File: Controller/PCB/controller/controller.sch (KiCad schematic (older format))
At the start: 66 parts

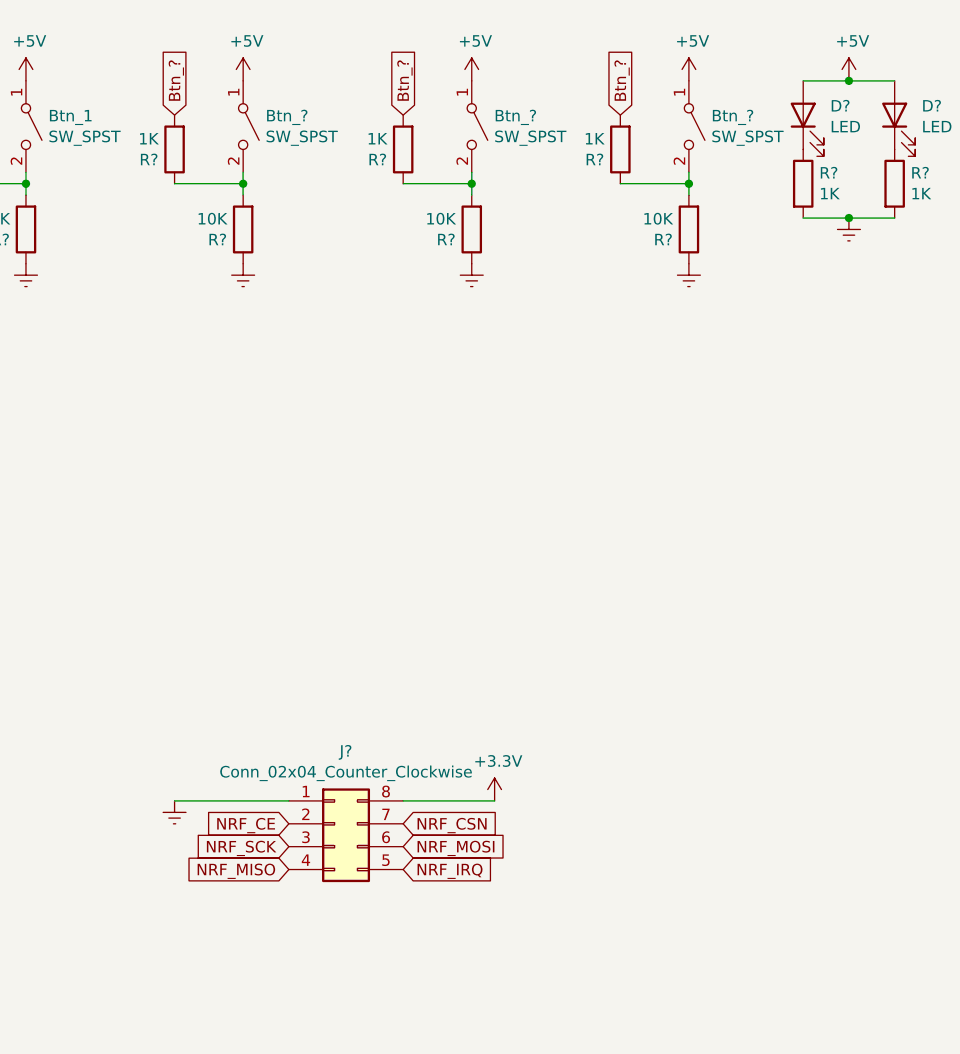
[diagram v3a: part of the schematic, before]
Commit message: Update 2 of the buttons into switches
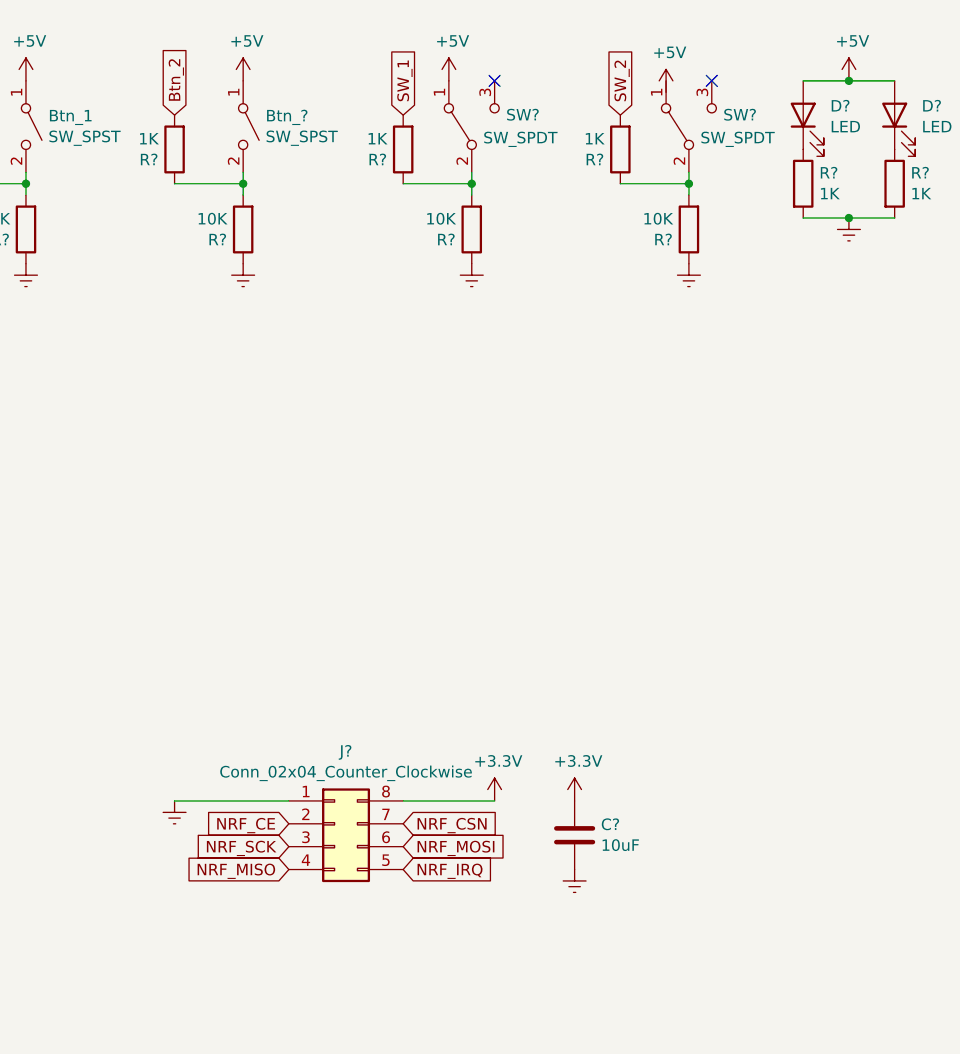
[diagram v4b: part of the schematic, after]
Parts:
- removed Btn_? (x2): SW_SPST, symbol Switch:SW_SPST
- added C?: 10uF, symbol Device:C
- added SW? (x2): SW_SPDT, symbol Switch:SW_SPDT
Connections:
- net +3V3: now also C?.1
- net +5V: now also SW?.1 (A)
- net Earth: now also C?.2
- net at R?.1, R?.2: now also SW?.2 (B) (x2)
- removed net Btn_?: R?.2, R?.2, R?.2
- new net Btn_2: R?.2
- new net SW_1: R?.2
- new net SW_2: R?.2
- no-connect marks 1 -> 3
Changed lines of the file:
@@
 $EndComp
 Text GLabel 6000 900  1    50   Input ~ 0
-Btn_?
+Btn_2
 $Comp
 L power:Earth #PWR?
@@
 Connection ~ 6300 1200
 $Comp
-L Switch:SW_SPST Btn_?
-U 1 1 6210AEE9
-P 7300 950
-F 0 "Btn_?" V 7254 1048 50  0000 L CNN
-F 1 "SW_SPST" V 7345 1048 50  0000 L CNN
-F 2 "" H 7300 950 50  0001 C CNN
-F 3 "~" H 7300 950 50  0001 C CNN
-	1    7300 950
-	0    1    1    0
-$EndComp
-$Comp
 L Device:R R?
 U 1 1 6210AEEF
@@
 $EndComp
 Text GLabel 7000 900  1    50   Input ~ 0
-Btn_?
+SW_1
 $Comp
 L power:Earth #PWR?
@@
 Connection ~ 7300 1200
 $Comp
-L Switch:SW_SPST Btn_?
-U 1 1 6210CFFF
-P 8250 950
-F 0 "Btn_?" V 8204 1048 50  0000 L CNN
-F 1 "SW_SPST" V 8295 1048 50  0000 L CNN
-F 2 "" H 8250 950 50  0001 C CNN
-F 3 "~" H 8250 950 50  0001 C CNN
-	1    8250 950
-	0    1    1    0
-$EndComp
-$Comp
 L Device:R R?
 U 1 1 6210D005
@@
 $EndComp
 Text GLabel 7950 900  1    50   Input ~ 0
-Btn_?
+SW_2
 $Comp
 L power:Earth #PWR?
@@
 L power:+5V #PWR?
 U 1 1 6208E5D4
-P 8250 750
-F 0 "#PWR?" H 8250 600 50  0001 C CNN
-F 1 "+5V" H 8265 923 50  0000 C CNN
-F 2 "" H 8250 750 50  0001 C CNN
-F 3 "" H 8250 750 50  0001 C CNN
-	1    8250 750
+P 8150 800
+F 0 "#PWR?" H 8150 650 50  0001 C CNN
+F 1 "+5V" H 8165 973 50  0000 C CNN
+F 2 "" H 8150 800 50  0001 C CNN
+F 3 "" H 8150 800 50  0001 C CNN
+	1    8150 800
 	1    0    0    -1
 $EndComp
@@
 L power:+5V #PWR?
 U 1 1 62091695
-P 7300 750
-F 0 "#PWR?" H 7300 600 50  0001 C CNN
-F 1 "+5V" H 7315 923 50  0000 C CNN
-F 2 "" H 7300 750 50  0001 C CNN
-F 3 "" H 7300 750 50  0001 C CNN
-	1    7300 750
+P 7200 750
+F 0 "#PWR?" H 7200 600 50  0001 C CNN
+F 1 "+5V" H 7215 923 50  0000 C CNN
+F 2 "" H 7200 750 50  0001 C CNN
+F 3 "" H 7200 750 50  0001 C CNN
+	1    7200 750
 	1    0    0    -1
 $EndComp
@@
 Text GLabel 7000 4000 2    50   Input ~ 0
 NRF_CSN
+$Comp
+L power:+3.3V #PWR?
+U 1 1 620F525F
+P 7750 3900
+F 0 "#PWR?" H 7750 3750 50  0001 C CNN
+F 1 "+3.3V" H 7765 4073 50  0000 C CNN
+F 2 "" H 7750 3900 50  0001 C CNN
+F 3 "" H 7750 3900 50  0001 C CNN
+	1    7750 3900
+	1    0    0    -1
+$EndComp
+$Comp
+L Device:C C?
+U 1 1 620F58B9
+P 7750 4050
+F 0 "C?" H 7865 4096 50  0000 L CNN
+F 1 "10uF" H 7865 4005 50  0000 L CNN
+F 2 "" H 7788 3900 50  0001 C CNN
+F 3 "~" H 7750 4050 50  0001 C CNN
+	1    7750 4050
+	1    0    0    -1
+$EndComp
+$Comp
+L power:Earth #PWR?
+U 1 1 620F67B9
+P 7750 4200
+F 0 "#PWR?" H 7750 3950 50  0001 C CNN
+F 1 "Earth" H 7750 4050 50  0001 C CNN
+F 2 "" H 7750 4200 50  0001 C CNN
+F 3 "~" H 7750 4200 50  0001 C CNN
+	1    7750 4200
+	1    0    0    -1
+$EndComp
+$Comp
+L Switch:SW_SPDT SW?
+U 1 1 620F8D01
+P 7300 950
+F 0 "SW?" V 7350 800 50  0000 R CNN
+F 1 "SW_SPDT" V 7250 900 50  0000 R CNN
+F 2 "" H 7300 950 50  0001 C CNN
+F 3 "~" H 7300 950 50  0001 C CNN
+	1    7300 950
+	0    -1   -1   0
+$EndComp
+$Comp
+L Switch:SW_SPDT SW?
+U 1 1 620FA2D7
+P 8250 950
+F 0 "SW?" V 8300 800 50  0000 R CNN
+F 1 "SW_SPDT" V 8200 900 50  0000 R CNN
+F 2 "" H 8250 950 50  0001 C CNN
+F 3 "~" H 8250 950 50  0001 C CNN
+	1    8250 950
+	0    -1   -1   0
+$EndComp
+NoConn ~ 8350 750
+NoConn ~ 7400 750
 $EndSCHEMATC

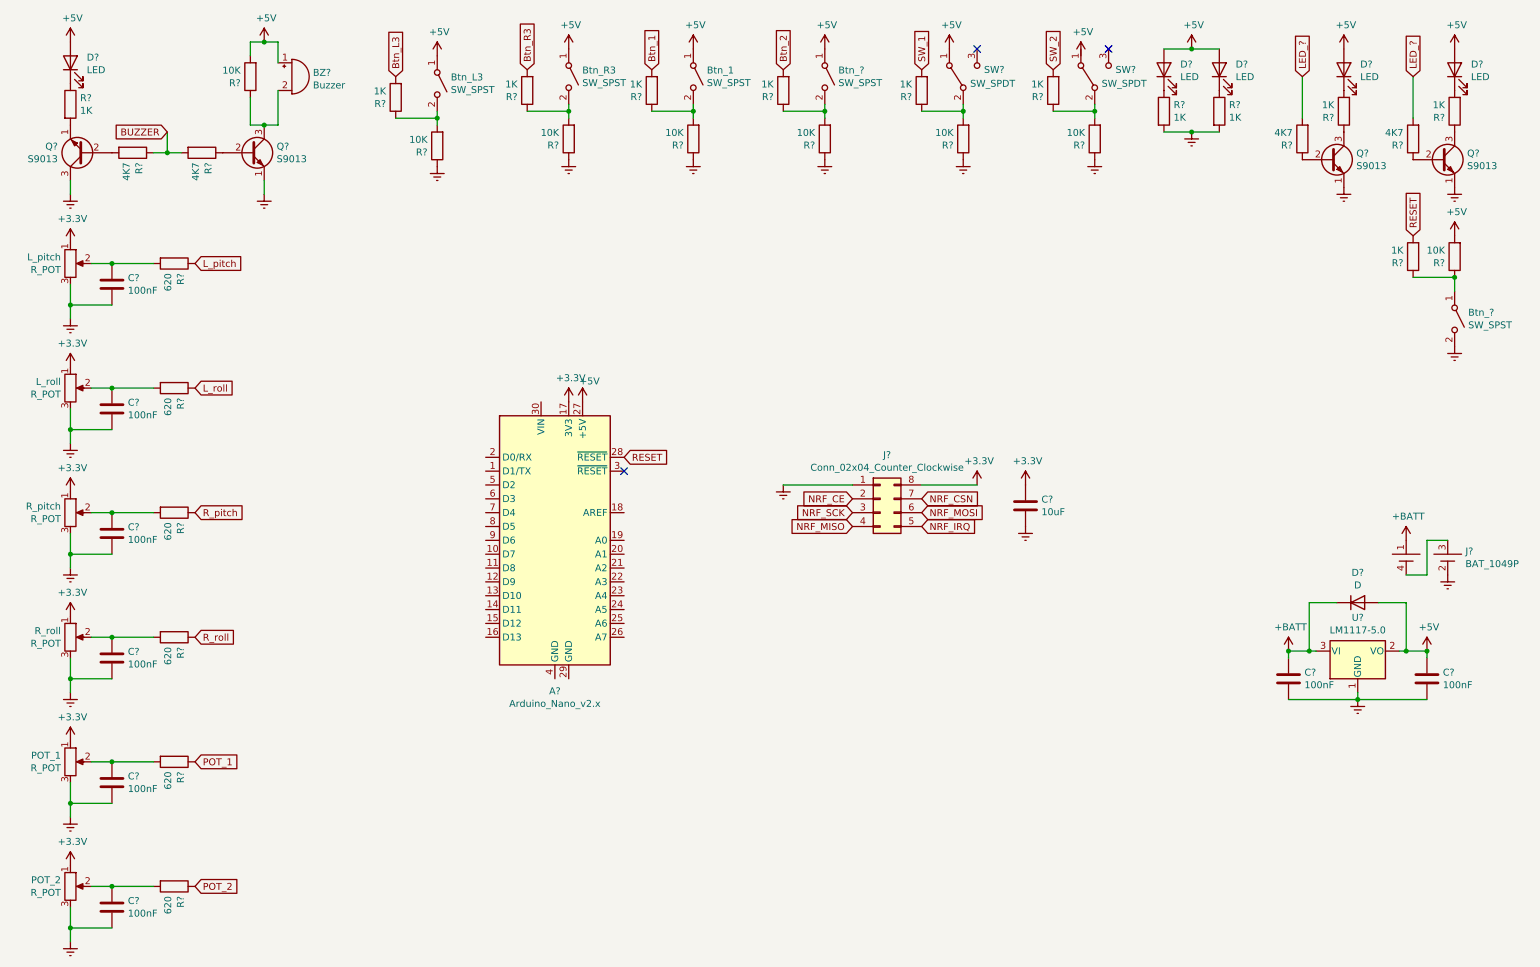
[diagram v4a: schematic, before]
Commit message: Added Joysticks to schematic
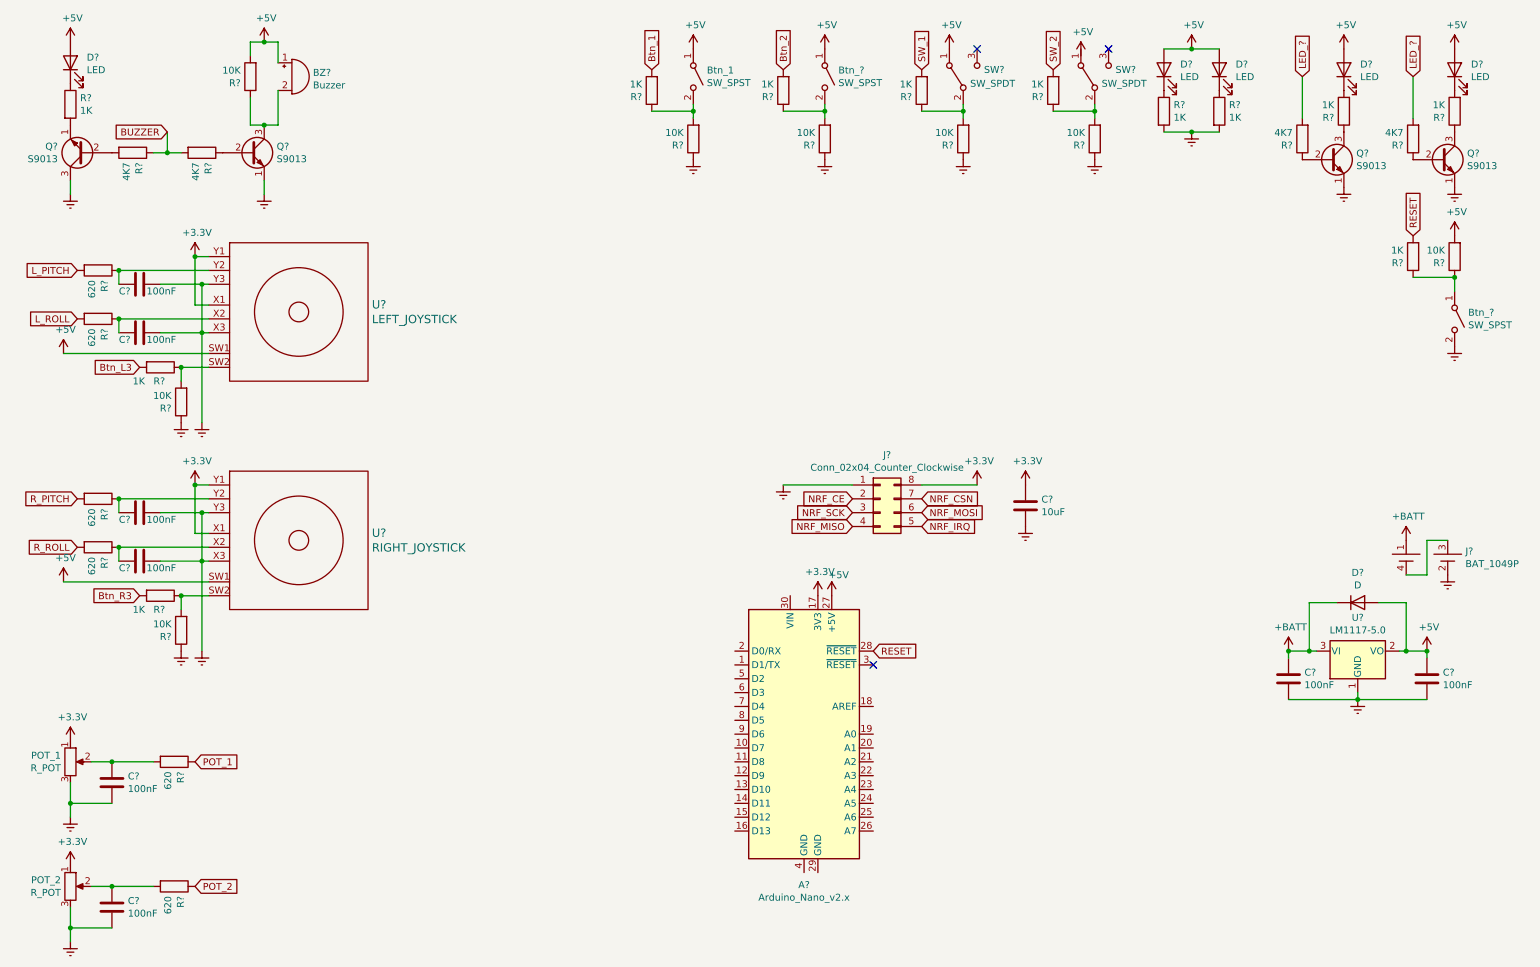
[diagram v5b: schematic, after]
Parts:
- removed Btn_L3, Btn_R3: SW_SPST, symbol Switch:SW_SPST
- removed C? (x4): 100nF, symbol Device:C
- removed L_pitch, L_roll, R_pitch, R_roll: R_POT, symbol Device:R_POT
- removed R? (x4): 620, symbol Device:R
- removed R?: 1K, symbol Device:R
- removed R?: 10K, symbol Device:R
- added C? (x4): 100nF, symbol Device:C
- added R? (x4): 620, symbol Device:R
- added R?: 1K, symbol Device:R
- added R?: 10K, symbol Device:R
- added U?: LEFT_JOYSTICK, symbol TickerForge:JOYSTICK_BUTTON
- added U?: RIGHT_JOYSTICK, symbol TickerForge:JOYSTICK_BUTTON
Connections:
- net +3V3: now also U?.X1, U?.X1, U?.Y1, U?.Y1
- net +5V: now also U?.SW1, U?.SW1
- net Btn_R3: now also R?.2
- net Earth: now also C?.1, C?.1, C?.1, C?.1, R?.1, U?.X3, U?.X3, U?.Y3, U?.Y3
- net at R?.1, R?.2: now also U?.SW2
- new net: C?.2, R?.1, U?.X2 (x2)
- new net: C?.2, R?.1, U?.Y2 (x2)
- new net: R?.1, R?.2, U?.SW2
- new net L_PITCH: R?.2
- new net L_ROLL: R?.2
- new net R_PITCH: R?.2
- new net R_ROLL: R?.2
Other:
- moved on the sheet: A?, R?
